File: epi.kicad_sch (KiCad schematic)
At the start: 27 parts, among them J1 Conn_01x12, J2 Conn_01x12, J3 Conn_01x04, J4 USB_C_Receptacle_USB2.0, U1 ATmega32U4-M, Y1 16mhz

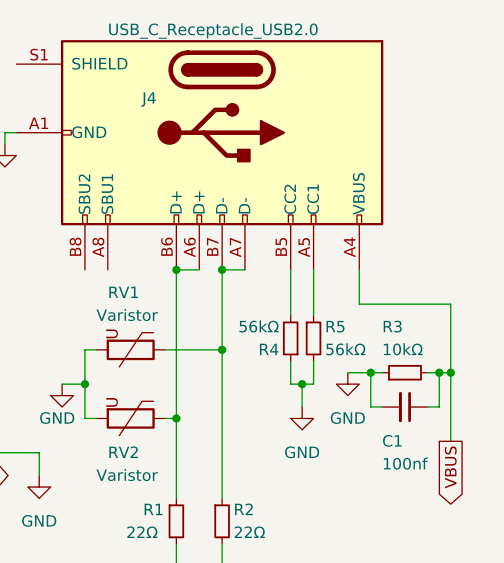
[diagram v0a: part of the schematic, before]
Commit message: redesign, added fuse
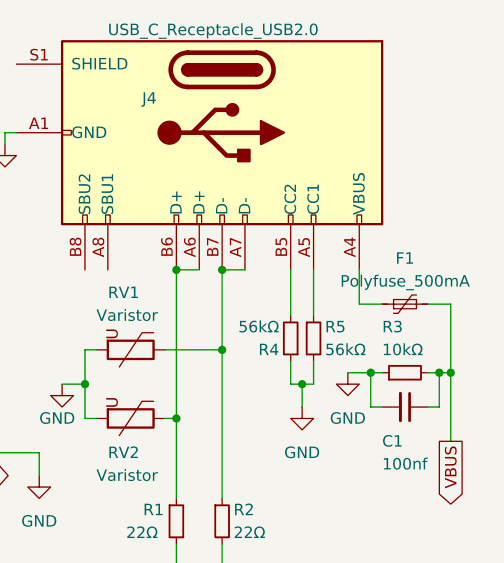
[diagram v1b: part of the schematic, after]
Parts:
- added F1: Polyfuse_500mA, Fuse:Fuse_0402_1005Metric, symbol Device:Polyfuse_Small
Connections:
- net +5V: now also F1.2; no longer J4.A4 (VBUS), J4.A9 (VBUS), J4.B4 (VBUS), J4.B9 (VBUS)
- new net: F1.1, J4.A4 (VBUS), J4.A9 (VBUS), J4.B4 (VBUS), J4.B9 (VBUS)
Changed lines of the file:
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@@
+    (stroke (width 0) (type default) (color 0 0 0 0))
+  )
+  (wire (pts (xy 187.96 44.45) (xy 185.42 44.45))
     (stroke (width 0) (type default) (color 0 0 0 0))
   )
@@
     (stroke (width 0) (type default) (color 0 0 0 0))
   )
-  (wire (pts (xy 195.58 44.45) (xy 185.42 44.45))
+  (wire (pts (xy 195.58 44.45) (xy 193.04 44.45))
     (stroke (width 0) (type default) (color 0 0 0 0))
   )
@@
     )
     (pin "1")
+  )
+  (symbol (lib_id "Device:Polyfuse_Small") (at 190.5 44.45 90) (unit 1)
+    (in_bom yes) (on_board yes)
+    (property "Reference" "F1" (id 0) (at 190.5 39.37 90))
+    (property "Value" "Polyfuse_500mA" (id 1) (at 190.5 41.91 90))
+    (property "Footprint" "Fuse:Fuse_0402_1005Metric" (id 2) (at 195.58 43.18 0)
+      (effects (font (size 1.27 1.27)) (justify left) hide)
+    )
+    (property "Datasheet" "~" (id 3) (at 190.5 44.45 0)
+      (effects (font (size 1.27 1.27)) hide)
+    )
+    (pin "1")
+    (pin "2")
   )
   (symbol (lib_id "MCU_Microchip_ATmega:ATmega32U4-M") (at 60.96 78.74 0) (unit 1)
@@
       (reference "D2") (unit 1) (value "LED_Small") (footprint "LED_SMD:LED_0402_1005Metric")
     )
+    (path "/dda1dc04-f3c6-41f3-a456-12090ddf6a3a"
+      (reference "F1") (unit 1) (value "Polyfuse_500mA") (footprint "Fuse:Fuse_0402_1005Metric")
+    )
     (path "/2bf7c2a7-1ea3-4592-a226-b942f45a6bdb"

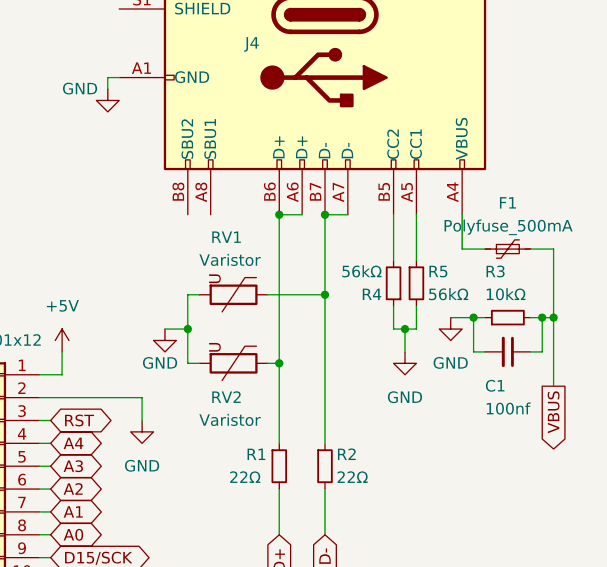
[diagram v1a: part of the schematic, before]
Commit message: fixed small USB port inaccuracy
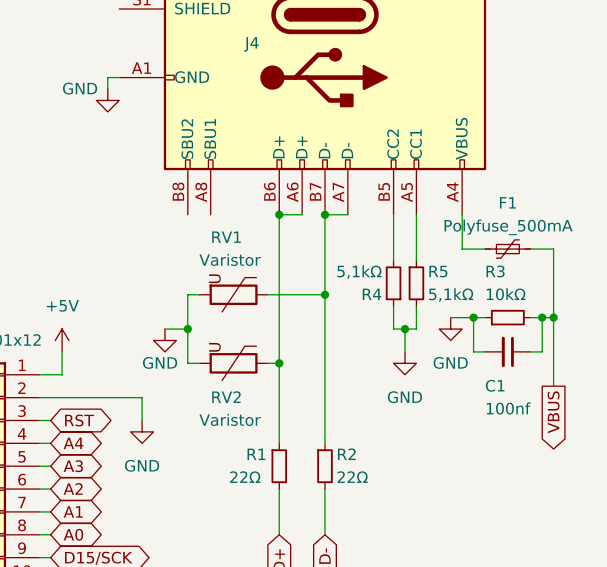
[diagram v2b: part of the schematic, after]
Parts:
- R4, R5: value 56kΩ -> 5,1kΩ
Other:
- company: (none) -> Rasmus L.
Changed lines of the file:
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@@
     (title "\"Epi\"")
     (date "2022-10-26")
+    (rev "1,1")
+    (company "Rasmus L.")
   )
   (junction (at 31.75 45.72) (diameter 0) (color 0 0 0 0)
@@
       (effects (font (size 1.27 1.27)) (justify left))
     )
-    (property "Value" "56kΩ" (id 1) (at 176.53 46.99 0)
+    (property "Value" "5,1kΩ" (id 1) (at 176.53 46.99 0)
       (effects (font (size 1.27 1.27)) (justify left))
     )
@@
       (effects (font (size 1.27 1.27)) (justify left))
     )
-    (property "Value" "56kΩ" (id 1) (at 181.61 49.53 0)
+    (property "Value" "5,1kΩ" (id 1) (at 181.61 49.53 0)
       (effects (font (size 1.27 1.27)) (justify left))
     )
@@
     )
     (path "/0838f439-92c2-4ce5-ba9d-37a51f08a736"
-      (reference "R4") (unit 1) (value "56kΩ") (footprint "Resistor_SMD:R_0402_1005Metric")
+      (reference "R4") (unit 1) (value "5,1kΩ") (footprint "Resistor_SMD:R_0402_1005Metric")
     )
     (path "/7bd5b29c-7a41-464f-bc71-c4d9335a750d"
-      (reference "R5") (unit 1) (value "56kΩ") (footprint "Resistor_SMD:R_0402_1005Metric")
+      (reference "R5") (unit 1) (value "5,1kΩ") (footprint "Resistor_SMD:R_0402_1005Metric")
     )
     (path "/5e35bf4c-7ada-442b-8ca6-c06dd0404eb2"

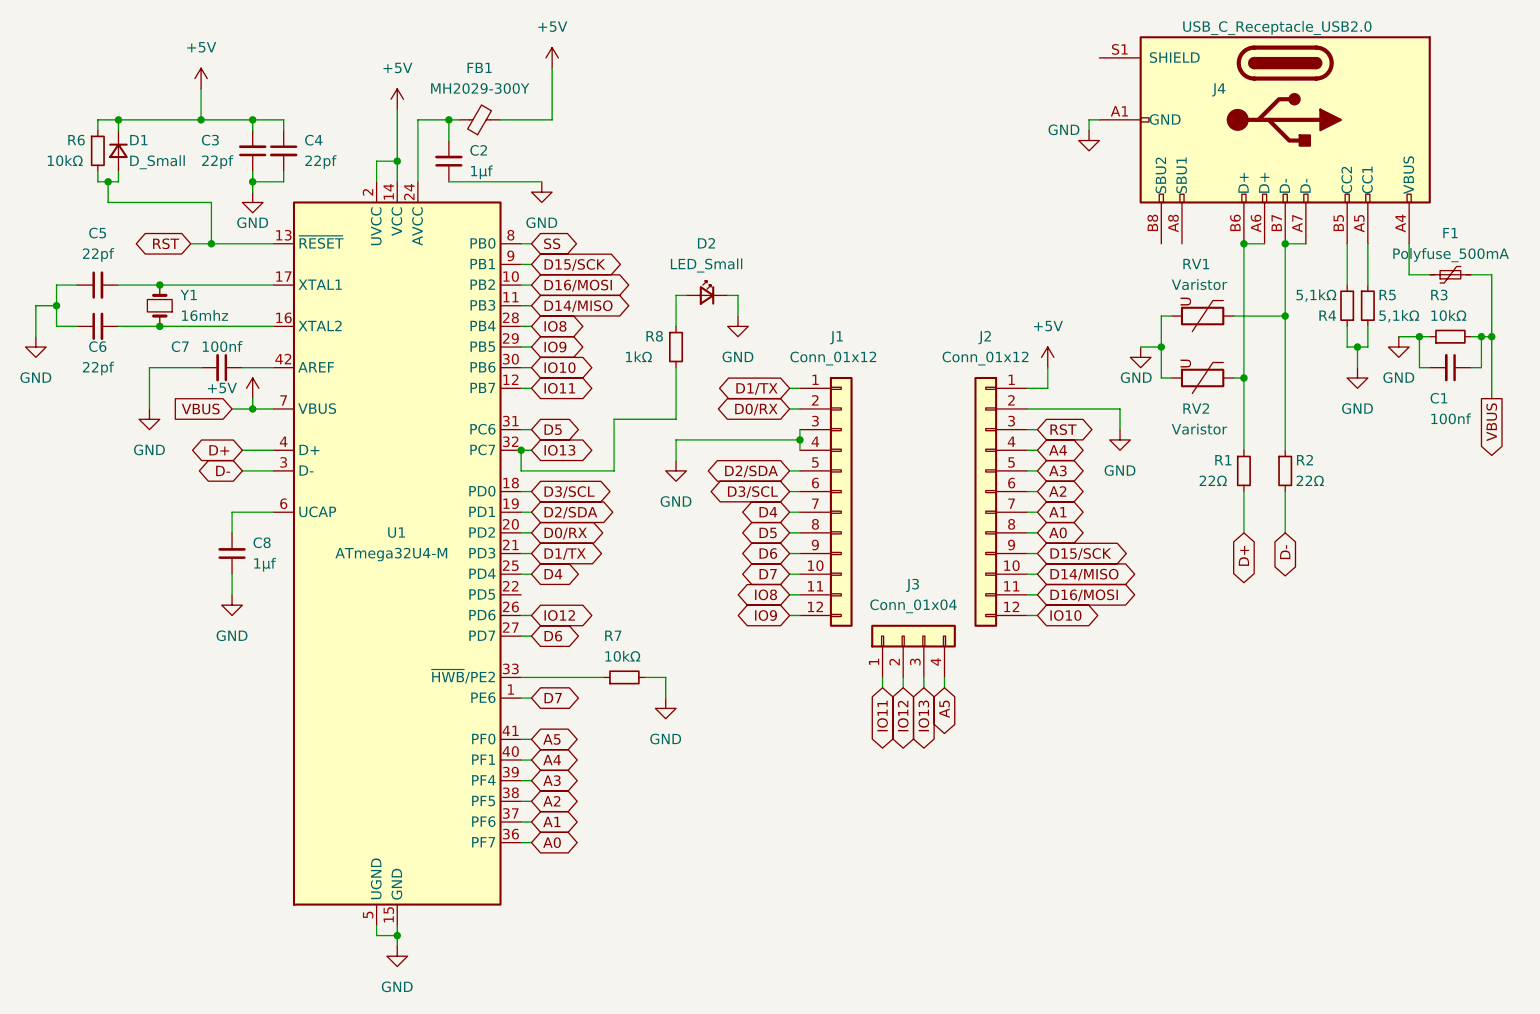
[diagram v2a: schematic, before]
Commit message: more descriptive part names and better BOM
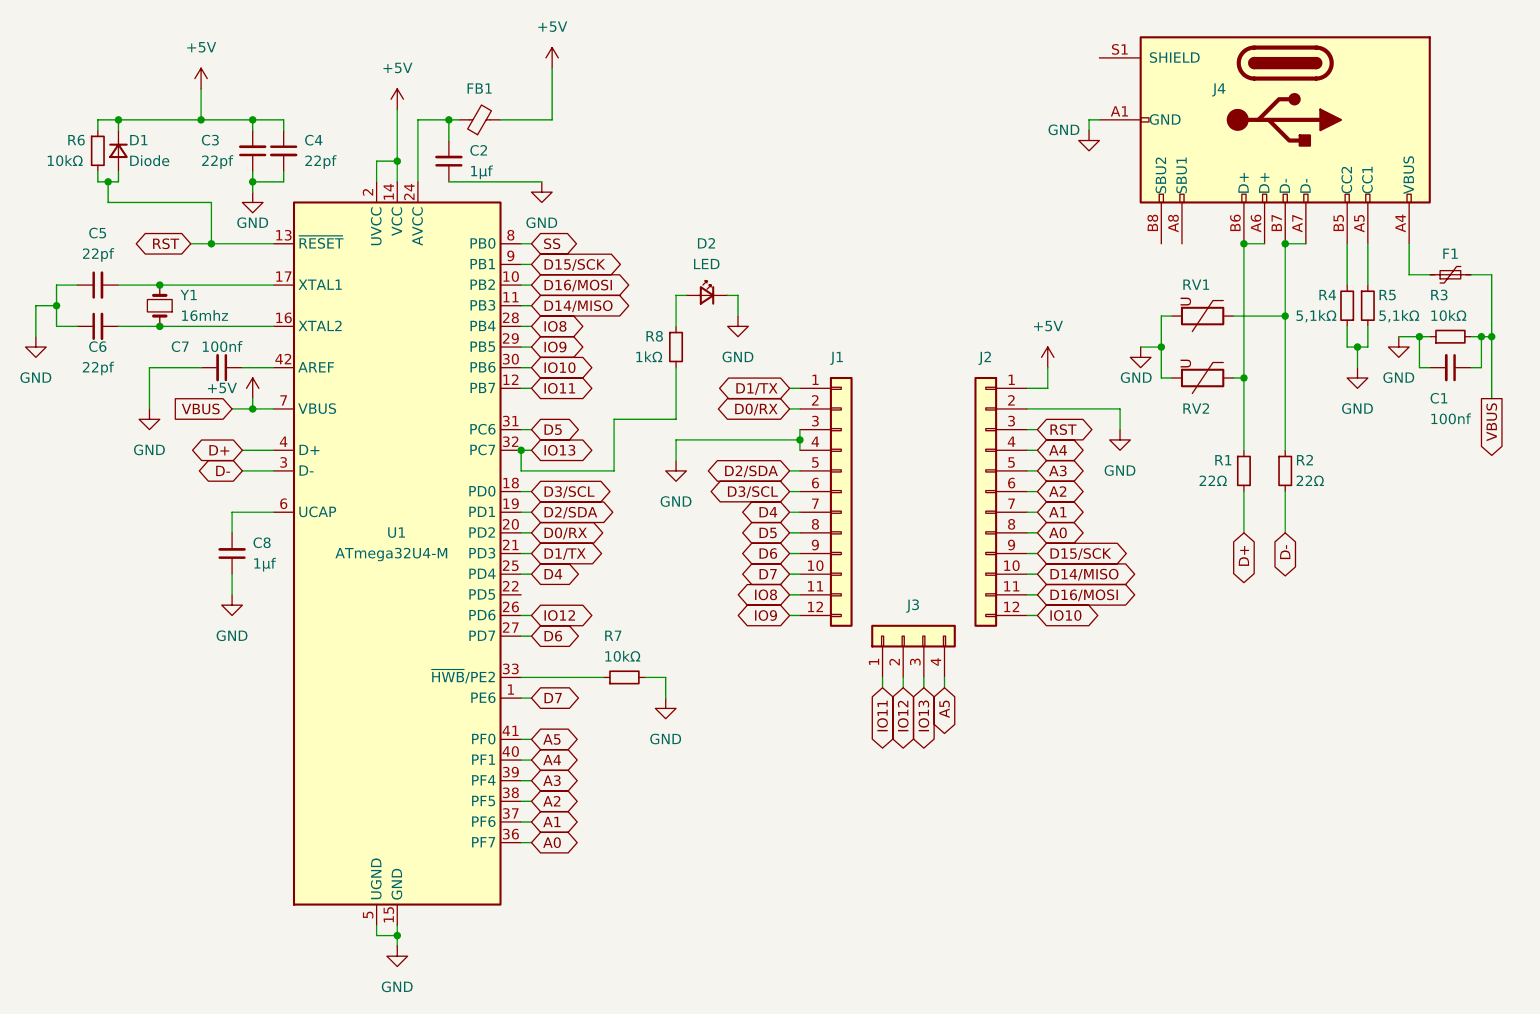
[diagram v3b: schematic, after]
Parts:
- D1: value D_Small -> Diode
- D2: value LED_Small -> LED
- F1: value Polyfuse_500mA -> Polyfuse 500mA HC
- FB1: value MH2029-300Y -> Ferrite bead low-pass filter
- J1, J2: value Conn_01x12 -> Connector 1x12
- J3: value Conn_01x04 -> Connector 1x04
- J4: value USB_C_Receptacle_USB2.0 -> USB-C 2.0 mid-mount female connector
- RV1, RV2: value Varistor -> ESD protection varistor
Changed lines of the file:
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@@
       (effects (font (size 1.27 1.27)) (justify left))
     )
-    (property "Value" "1kΩ" (id 1) (at 88.9 54.61 0)
+    (property "Value" "1kΩ" (id 1) (at 90.17 54.61 0)
       (effects (font (size 1.27 1.27)) (justify left))
     )
@@
   (symbol (lib_id "Device:R_Small") (at 177.8 48.26 180) (unit 1)
     (in_bom yes) (on_board yes)
-    (property "Reference" "R4" (id 0) (at 176.53 49.53 0)
-      (effects (font (size 1.27 1.27)) (justify left))
-    )
-    (property "Value" "5,1kΩ" (id 1) (at 176.53 46.99 0)
+    (property "Reference" "R4" (id 0) (at 176.53 46.99 0)
+      (effects (font (size 1.27 1.27)) (justify left))
+    )
+    (property "Value" "5,1kΩ" (id 1) (at 176.53 49.53 0)
       (effects (font (size 1.27 1.27)) (justify left))
     )
@@
   (symbol (lib_id "Device:FerriteBead_Small") (at 71.12 25.4 90) (unit 1)
     (in_bom yes) (on_board yes) (fields_autoplaced)
-    (property "Reference" "FB1" (id 0) (at 71.0819 19.05 90))
-    (property "Value" "MH2029-300Y" (id 1) (at 71.0819 21.59 90))
+    (property "Reference" "FB1" (id 0) (at 71.0819 21.59 90))
+    (property "Value" "Ferrite bead low-pass filter" (id 1) (at 71.0819 21.59 90)
+      (effects (font (size 1.27 1.27)) hide)
+    )
     (property "Footprint" "Resistor_SMD:R_0402_1005Metric" (id 2) (at 71.12 27.178 90)
       (effects (font (size 1.27 1.27)) hide)
@@
   (symbol (lib_id "Connector_Generic:Conn_01x04") (at 123.19 88.9 90) (unit 1)
     (in_bom yes) (on_board yes) (fields_autoplaced)
-    (property "Reference" "J3" (id 0) (at 124.46 82.55 90))
-    (property "Value" "Conn_01x04" (id 1) (at 124.46 85.09 90))
+    (property "Reference" "J3" (id 0) (at 124.46 85.09 90))
+    (property "Value" "Connector 1x04" (id 1) (at 124.46 85.09 90)
+      (effects (font (size 1.27 1.27)) hide)
+    )
     (property "Footprint" "Connector_PinHeader_1.27mm:PinHeader_1x04_P1.27mm_Vertical" (id 2) (at 123.19 88.9 0)
       (effects (font (size 1.27 1.27)) hide)
@@
   (symbol (lib_id "Connector_Generic:Conn_01x12") (at 133.35 71.12 0) (mirror y) (unit 1)
     (in_bom yes) (on_board yes) (fields_autoplaced)
-    (property "Reference" "J2" (id 0) (at 133.35 52.07 0))
-    (property "Value" "Conn_01x12" (id 1) (at 133.35 54.61 0))
+    (property "Reference" "J2" (id 0) (at 133.35 54.61 0))
+    (property "Value" "Connector 1x12" (id 1) (at 133.35 54.61 0)
+      (effects (font (size 1.27 1.27)) hide)
+    )
     (property "Footprint" "Connector_PinHeader_1.27mm:PinHeader_1x12_P1.27mm_Vertical" (id 2) (at 133.35 71.12 0)
       (effects (font (size 1.27 1.27)) hide)
@@
       (effects (font (size 1.27 1.27)) (justify left))
     )
-    (property "Value" "Varistor" (id 1) (at 156.21 63.5 90)
-      (effects (font (size 1.27 1.27)) (justify left))
+    (property "Value" "ESD protection varistor" (id 1) (at 156.21 63.5 90)
+      (effects (font (size 1.27 1.27)) (justify left) hide)
     )
     (property "Footprint" "Resistor_SMD:R_0402_1005Metric" (id 2) (at 160.02 55.372 90)
@@
     (in_bom yes) (on_board yes) (fields_autoplaced)
     (property "Reference" "D2" (id 0) (at 98.9965 40.64 0))
-    (property "Value" "LED_Small" (id 1) (at 98.9965 43.18 0))
+    (property "Value" "LED" (id 1) (at 98.9965 43.18 0))
     (property "Footprint" "LED_SMD:LED_0402_1005Metric" (id 2) (at 99.06 46.99 90)
       (effects (font (size 1.27 1.27)) hide)
@@
       (effects (font (size 1.27 1.27)) (justify left))
     )
-    (property "Value" "USB_C_Receptacle_USB2.0" (id 1) (at 157.48 13.97 90)
-      (effects (font (size 1.27 1.27)) (justify left))
+    (property "Value" "USB-C 2.0 mid-mount female connector" (id 1) (at 157.48 13.97 90)
+      (effects (font (size 1.27 1.27)) (justify left) hide)
     )
     (property "Footprint" "USB-C-Connectors-master:USB-C MC-314C-4P16" (id 2) (at 170.18 29.21 0)
@@
   (symbol (lib_id "Device:Polyfuse_Small") (at 190.5 44.45 90) (unit 1)
     (in_bom yes) (on_board yes)
-    (property "Reference" "F1" (id 0) (at 190.5 39.37 90))
-    (property "Value" "Polyfuse_500mA" (id 1) (at 190.5 41.91 90))
+    (property "Reference" "F1" (id 0) (at 190.5 41.91 90))
+    (property "Value" "Polyfuse 500mA HC" (id 1) (at 190.5 41.91 90)
+      (effects (font (size 1.27 1.27)) hide)
+    )
     (property "Footprint" "Fuse:Fuse_0402_1005Metric" (id 2) (at 195.58 43.18 0)
       (effects (font (size 1.27 1.27)) (justify left) hide)
@@
       (effects (font (size 1.27 1.27)) (justify left))
     )
-    (property "Value" "D_Small" (id 1) (at 27.94 30.48 90)
+    (property "Value" "Diode" (id 1) (at 27.94 30.48 90)
       (effects (font (size 1.27 1.27)) (justify left))
     )
@@
   (symbol (lib_id "Device:Varistor") (at 160.02 49.53 270) (unit 1)
     (in_bom yes) (on_board yes)
-    (property "Reference" "RV1" (id 0) (at 157.48 43.18 90)
-      (effects (font (size 1.27 1.27)) (justify left))
-    )
-    (property "Value" "Varistor" (id 1) (at 156.21 45.72 90)
-      (effects (font (size 1.27 1.27)) (justify left))
+    (property "Reference" "RV1" (id 0) (at 157.48 45.72 90)
+      (effects (font (size 1.27 1.27)) (justify left))
+    )
+    (property "Value" "ESD protection varistor" (id 1) (at 156.21 45.72 90)
+      (effects (font (size 1.27 1.27)) (justify left) hide)
     )
     (property "Footprint" "Resistor_SMD:R_0402_1005Metric" (id 2) (at 160.02 47.752 90)
@@
   (symbol (lib_id "Connector_Generic:Conn_01x12") (at 115.57 71.12 0) (unit 1)
     (in_bom yes) (on_board yes)
-    (property "Reference" "J1" (id 0) (at 114.3 52.07 0)
-      (effects (font (size 1.27 1.27)) (justify left))
-    )
-    (property "Value" "Conn_01x12" (id 1) (at 109.22 54.61 0)
-      (effects (font (size 1.27 1.27)) (justify left))
+    (property "Reference" "J1" (id 0) (at 114.3 54.61 0)
+      (effects (font (size 1.27 1.27)) (justify left))
+    )
+    (property "Value" "Connector 1x12" (id 1) (at 109.22 54.61 0)
+      (effects (font (size 1.27 1.27)) (justify left) hide)
     )
     (property "Footprint" "Connector_PinHeader_1.27mm:PinHeader_1x12_P1.27mm_Vertical" (id 2) (at 115.57 71.12 0)
@@
     )
     (path "/e7416661-ba9b-499d-8603-5221b2873cf5"
-      (reference "D1") (unit 1) (value "D_Small") (footprint "Diode_SMD:D_0402_1005Metric")
+      (reference "D1") (unit 1) (value "Diode") (footprint "Diode_SMD:D_0402_1005Metric")
     )
     (path "/a5c417ed-b498-4a7f-a657-0a9106b9a2d7"
-      (reference "D2") (unit 1) (value "LED_Small") (footprint "LED_SMD:LED_0402_1005Metric")
+      (reference "D2") (unit 1) (value "LED") (footprint "LED_SMD:LED_0402_1005Metric")
     )
     (path "/dda1dc04-f3c6-41f3-a456-12090ddf6a3a"
-      (reference "F1") (unit 1) (value "Polyfuse_500mA") (footprint "Fuse:Fuse_0402_1005Metric")
+      (reference "F1") (unit 1) (value "Polyfuse 500mA HC") (footprint "Fuse:Fuse_0402_1005Metric")
     )
     (path "/2bf7c2a7-1ea3-4592-a226-b942f45a6bdb"
-      (reference "FB1") (unit 1) (value "MH2029-300Y") (footprint "Resistor_SMD:R_0402_1005Metric")
+      (reference "FB1") (unit 1) (value "Ferrite bead low-pass filter") (footprint "Resistor_SMD:R_0402_1005Metric")
     )
     (path "/fd8391ba-6477-49f1-90ad-f0984adfcfe9"
-      (reference "J1") (unit 1) (value "Conn_01x12") (footprint "Connector_PinHeader_1.27mm:PinHeader_1x12_P1.27mm_Vertical")
+      (reference "J1") (unit 1) (value "Connector 1x12") (footprint "Connector_PinHeader_1.27mm:PinHeader_1x12_P1.27mm_Vertical")
     )
     (path "/4025df47-50d6-4380-9774-3125e5050d74"
-      (reference "J2") (unit 1) (value "Conn_01x12") (footprint "Connector_PinHeader_1.27mm:PinHeader_1x12_P1.27mm_Vertical")
+      (reference "J2") (unit 1) (value "Connector 1x12") (footprint "Connector_PinHeader_1.27mm:PinHeader_1x12_P1.27mm_Vertical")
     )
     (path "/2f1e7d29-8a9f-4df0-a5ed-3038c787022d"
-      (reference "J3") (unit 1) (value "Conn_01x04") (footprint "Connector_PinHeader_1.27mm:PinHeader_1x04_P1.27mm_Vertical")
+      (reference "J3") (unit 1) (value "Connector 1x04") (footprint "Connector_PinHeader_1.27mm:PinHeader_1x04_P1.27mm_Vertical")
     )
     (path "/d4504eaf-f037-4b62-92f8-72f7dc724739"
-      (reference "J4") (unit 1) (value "USB_C_Receptacle_USB2.0") (footprint "USB-C-Connectors-master:USB-C MC-314C-4P16")
+      (reference "J4") (unit 1) (value "USB-C 2.0 mid-mount female connector") (footprint "USB-C-Connectors-master:USB-C MC-314C-4P16")
     )
     (path "/9b22129a-0dd2-4970-a0f6-8e9334734a40"
@@
     )
     (path "/ee341107-f8dd-4705-9401-8f8385a300c5"
-      (reference "RV1") (unit 1) (value "Varistor") (footprint "Resistor_SMD:R_0402_1005Metric")
+      (reference "RV1") (unit 1) (value "ESD protection varistor") (footprint "Resistor_SMD:R_0402_1005Metric")
     )
     (path "/7e3dc4a2-8186-4e1d-ae58-885c7591b8da"
-      (reference "RV2") (unit 1) (value "Varistor") (footprint "Resistor_SMD:R_0402_1005Metric")
+      (reference "RV2") (unit 1) (value "ESD protection varistor") (footprint "Resistor_SMD:R_0402_1005Metric")
     )
     (path "/e5a34e74-740d-4f11-ae22-b442e9a04463"
